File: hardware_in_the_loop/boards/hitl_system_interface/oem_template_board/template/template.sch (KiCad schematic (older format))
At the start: 40 parts, among them J1 CONN_02X03, J2 NanoFit_RA_SMT_08, U1 MCP2561-E_SN, U101 TPS560430YF, U2 ATMEGA16M1, U3 USB_MicroB, U4 FT232RL, Y1 Crystal_SMD

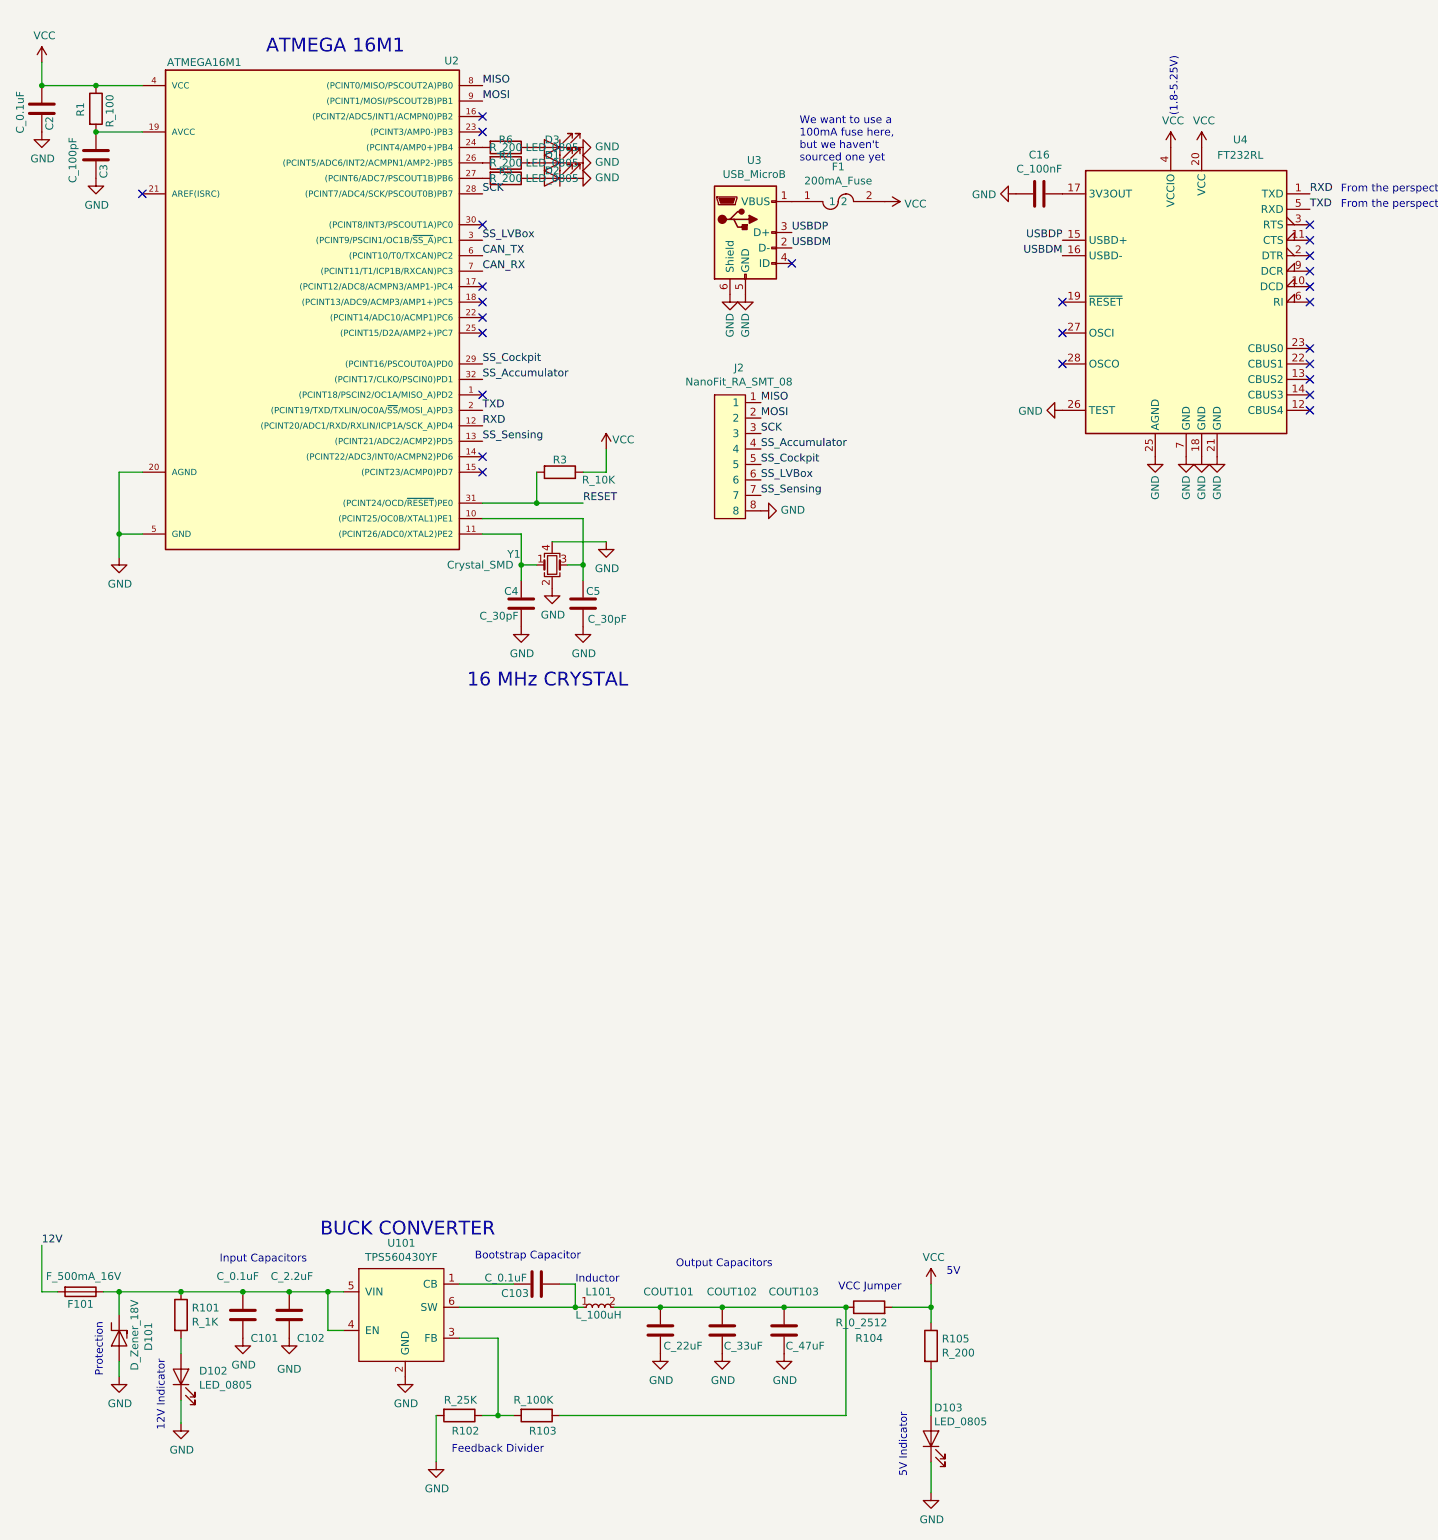
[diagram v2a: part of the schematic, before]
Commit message: Added capacitors to FT232RL and deleted the buck converter
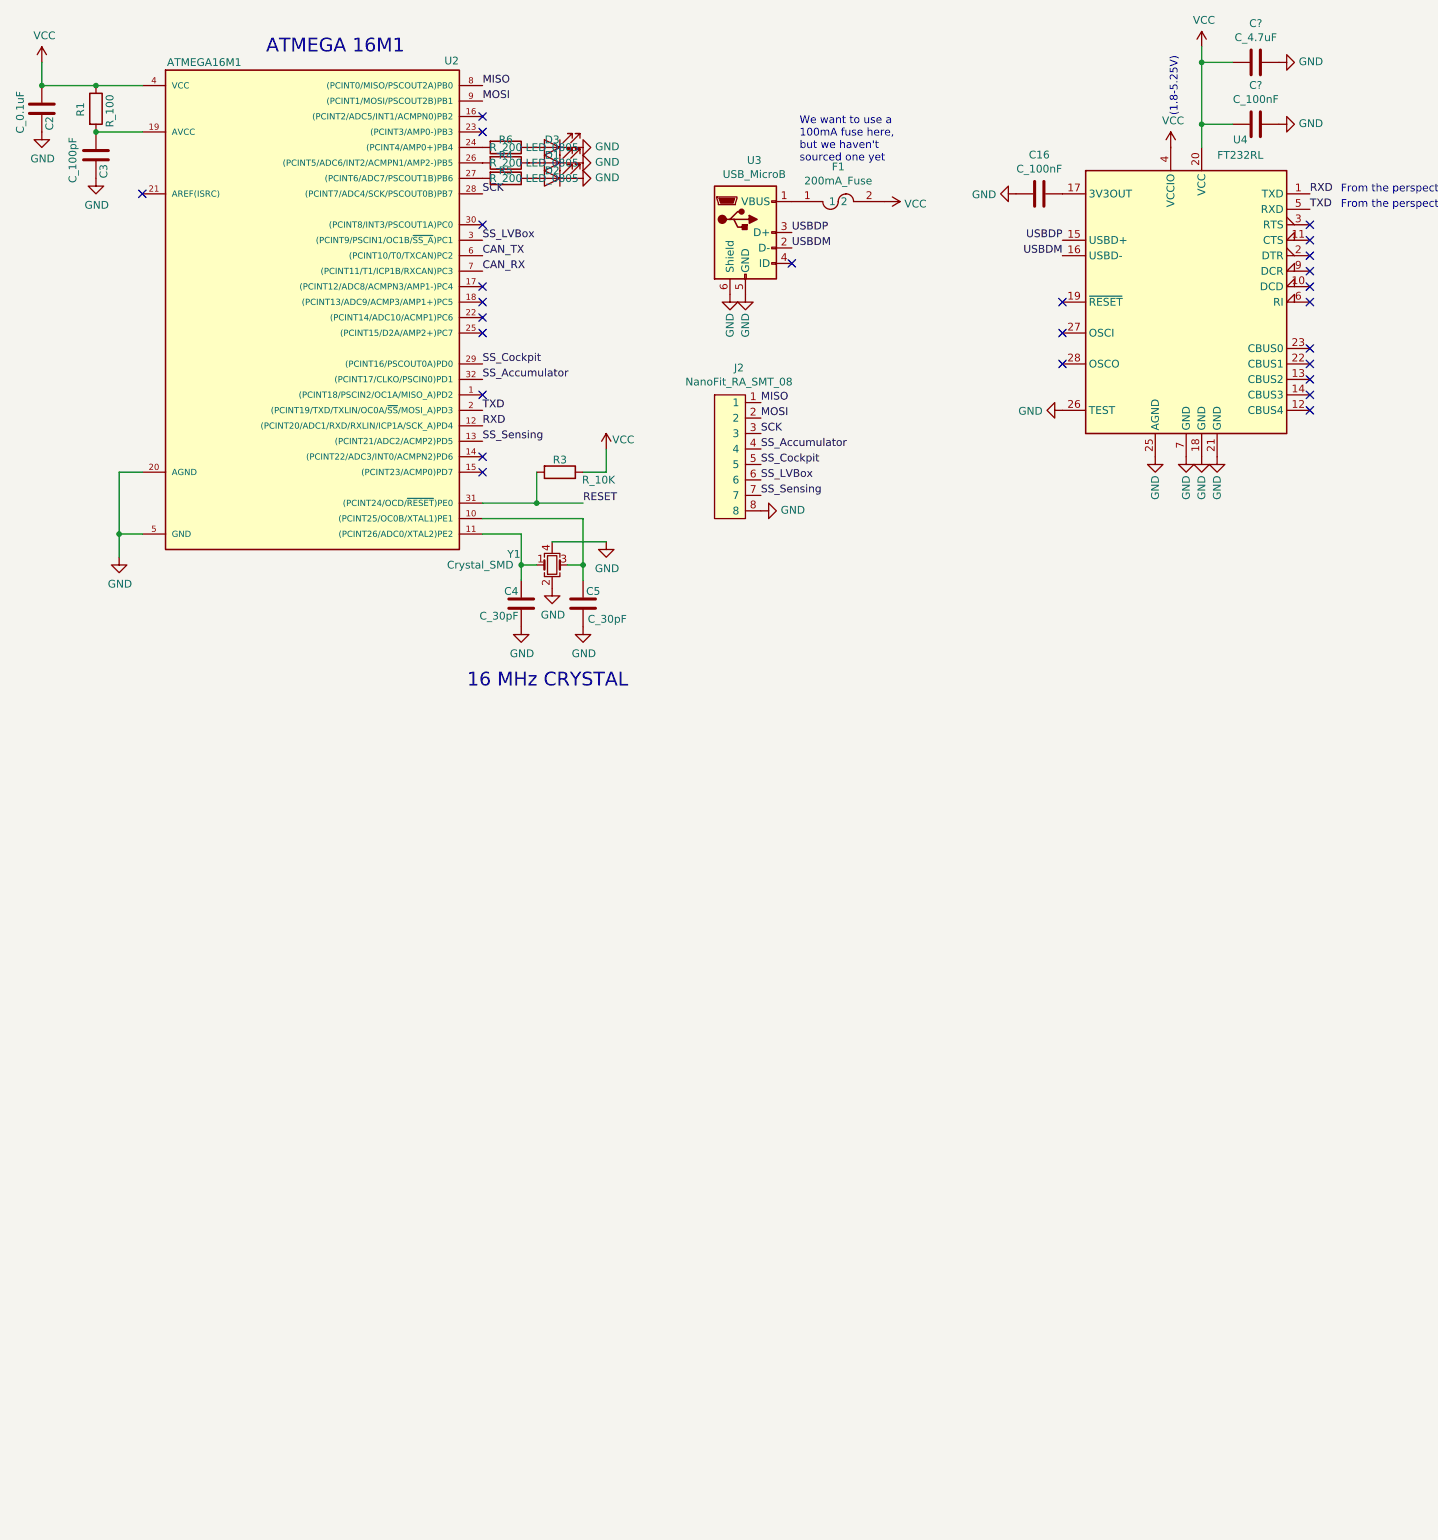
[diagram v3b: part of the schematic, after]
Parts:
- removed C101, C103: C_0.1uF, footprints:C_0805_OEM, symbol template-rescue:C_0.1uF-formula
- removed C102: C_2.2uF, footprints:C_0603_1608Metric, symbol template-rescue:C_2.2uF-formula
- removed COUT101: C_22uF, footprints:C_1206_OEM, symbol template-rescue:C_22uF-formula
- removed COUT102: C_33uF, footprints:Fuse_1812, symbol template-rescue:C_33uF-formula
- removed COUT103: C_47uF, footprints:C_0805_OEM, symbol template-rescue:C_47uF-formula
- removed D101: D_Zener_18V, footprints:DO-214AA, symbol template-rescue:D_Zener_18V-formula
- removed D102, D103: LED_0805, footprints:LED_0805_OEM, symbol template-rescue:LED_0805-formula
- removed F101: F_500mA_16V, footprints:Fuse_1210, symbol template-rescue:F_500mA_16V-formula
- removed L101: L_100uH, formula:L_100uH, symbol template-rescue:L_100uH-formula
- removed R101: R_1K, footprints:R_0805_OEM, symbol formula:R_1K
- removed R102: R_25K, footprints:R_0805_OEM, symbol template-rescue:R_25K-formula
- removed R103: R_100K, footprints:R_0805_OEM, symbol template-rescue:R_100K-formula
- removed R104: R_0_2512, footprints:R_2512_OEM, symbol template-rescue:R_0_2512-formula
- removed R105: R_200, footprints:R_0805_OEM, symbol template-rescue:R_200-formula
- removed U101: TPS560430YF, footprints:SOT-23-6_OEM, symbol template-rescue:TPS560430YF-formula
- added C?: C_4.7uF, footprints:C_0603_1608Metric, symbol formula:C_4.7uF
- added C?: C_100nF, footprints:C_0603_1608Metric, symbol formula:C_100nF
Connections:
- net GND: now also C?.1, C?.1
- net VCC: now also C?.2, C?.2
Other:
- note removed: "12V Indicator"
- note removed: "5V"
- note removed: "5V Indicator"
- note removed: "BUCK CONVERTER\n"
- note removed: "Bootstrap Capacitor\n"
- note removed: "Feedback Divider\n"
- note removed: "Inductor\n"
- note removed: "Input Capacitors\n\n"
- note removed: "Output Capacitors\n"
- note removed: "Protection\n"
- note removed: "VCC Jumper\n"

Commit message: Design Review Schematic
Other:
- note added: "Do not populate"
- moved on the sheet: C1, J1, R2, U1

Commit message: Copy of Design Review #1 Schematic
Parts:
- removed C16, C?: C_100nF, footprints:C_0603_1608Metric, symbol formula:C_100nF
- removed C?: C_4.7uF, footprints:C_0603_1608Metric, symbol formula:C_4.7uF
- removed D1, D2, D3: LED_0805, footprints:LED_0805_OEM, symbol formula:LED_0805
- removed F1: 200mA_Fuse, footprints:Fuse_1812, symbol formula:200mA_Fuse
- removed J2: NanoFit_RA_SMT_08, footprints:NanoFit_RA_8, symbol formula:NanoFit_RA_SMT_08
- removed R4, R5, R6: R_200, footprints:R_0805_OEM, symbol formula:R_200
- removed U3: USB_MicroB, Connectors_USB:USB_Micro-B_Molex-105017-0001, symbol formula:USB_MicroB
- removed U4: FT232RL, Package_SO:SSOP-28_5.3x10.2mm_P0.65mm, symbol formula:FT232RL
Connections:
- net CAN_RX: no longer U2.7 ((PCINT11/T1/ICP1B/RXCAN)PC3)
- net CAN_TX: no longer U2.6 ((PCINT10/T0/TXCAN)PC2)
- net MISO: no longer U2.8 ((PCINT0/MISO/PSCOUT2A)PB0)
- net MOSI: no longer U2.9 ((PCINT1/MOSI/PSCOUT2B)PB1)
- net SCK: no longer U2.28 ((PCINT7/ADC4/SCK/PSCOUT0B)PB7)
- net RXD: no longer names the net of U2.12 ((PCINT20/ADC1/RXD/RXLIN/ICP1A/SCK_A)PD4)
- net SS_Accumulator: no longer names the net of U2.32 ((PCINT17/CLKO/PSCIN0)PD1)
- net SS_Cockpit: no longer names the net of U2.29 ((PCINT16/PSCOUT0A)PD0)
- net SS_LVBox: no longer names the net of U2.3 ((PCINT9/PSCIN1/OC1B/~SS_A~)PC1)
- net SS_Sensing: no longer names the net of U2.13 ((PCINT21/ADC2/ACMP2)PD5)
- net TXD: no longer names the net of U2.2 ((PCINT19/TXD/TXLIN/OC0A/~SS~/MOSI_A)PD3)
- no-connect marks 27 -> 1
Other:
- note removed: "(1.8-5.25V)"
- note removed: "Do not populate"
- note removed: "From the perspective of the Atmega"
- note removed: "We want to use a \n100mA fuse here, \nbut we haven't \nsourced one yet\n"
- moved on the sheet: C1, J1, R2, U1
